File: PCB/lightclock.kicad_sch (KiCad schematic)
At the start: 187 parts, among them M1 Fan, Q1 NPN, Q2 AO3401A, Q3 AO3400A, SW1 TP15822637, U1 STP24DP05BTR, U11 TPS54232DR, U12 MPR121QR2, U13 PM254-1-06-W-8.5, U2 CH224K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

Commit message: added spare GPIO pads & ventilation for enclosure back
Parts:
- added GP24, GP25, GP26, GP27: ExtraGPIO, TestPoint:TestPoint_THTPad_1.5x1.5mm_Drill0.7mm, symbol Connector:TestPoint
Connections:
- net at U4.36 (GPIO24): now also GP24.1
- net at U4.37 (GPIO25): now also GP25.1
- net at U4.38 (GPIO26/ADC0): now also GP26.1
- net at U4.39 (GPIO27/ADC1): now also GP27.1
- no-connect marks 39 -> 35

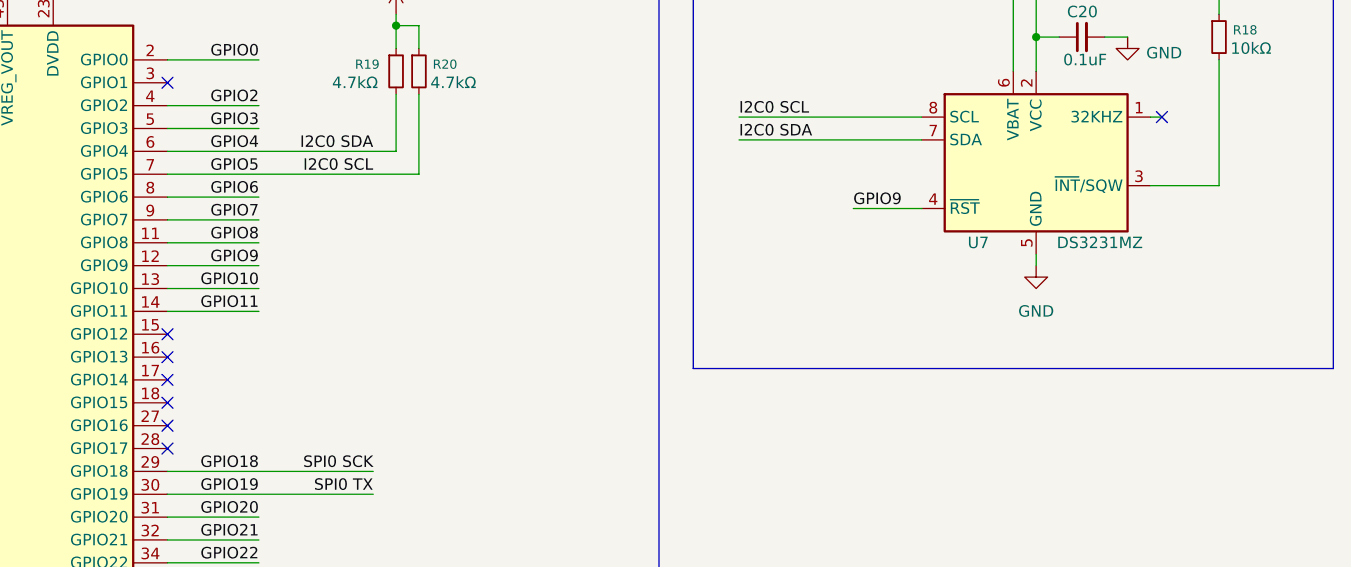
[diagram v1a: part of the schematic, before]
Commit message: connected INT pin on RTC to RP2040 for alarms
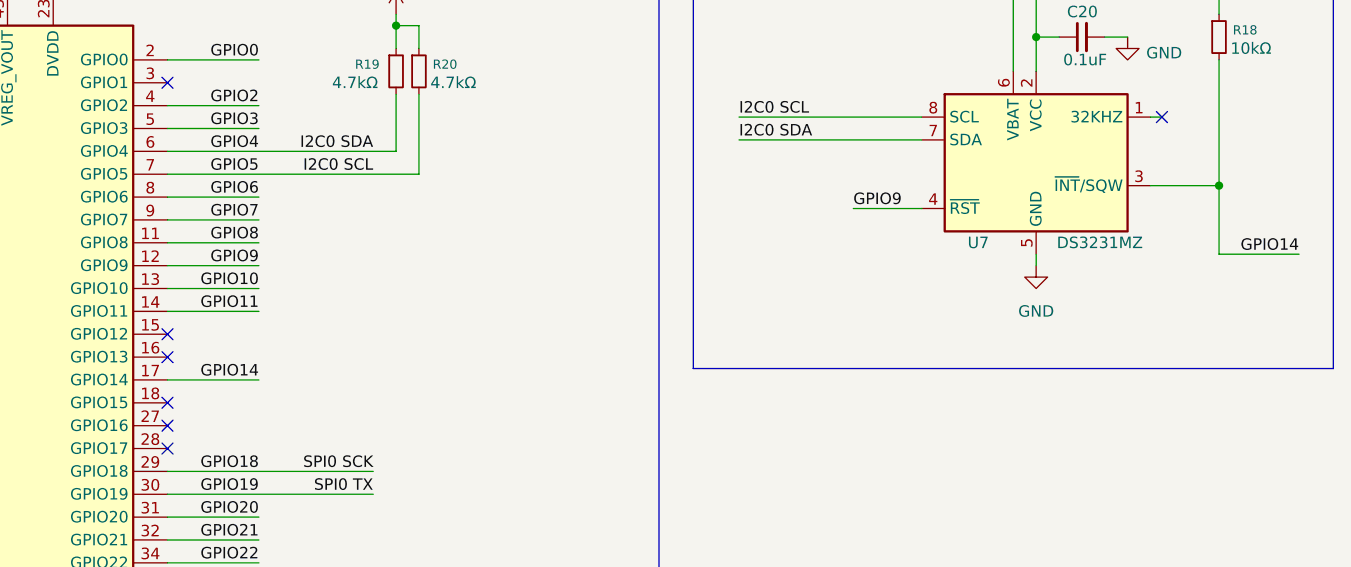
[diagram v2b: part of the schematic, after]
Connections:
- net GPIO14: now reaches R18.2, U7.3 (~{INT}/SQW)
- net GPIO14: now also U4.17 (GPIO14)
- no-connect marks 35 -> 34
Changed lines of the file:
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@@
 	)
 	(junction
+		(at 472.44 72.39)
+		(diameter 0)
+		(color 0 0 0 0)
+	)
+	(junction
 		(at 73.66 227.33)
 		(diameter 0)
@@
 	)
 	(no_connect
-		(at 355.6 93.98)
-	)
-	(no_connect
 		(at 435.61 210.82)
 	)
@@
 	(wire
 		(pts
+			(xy 365.76 93.98) (xy 355.6 93.98)
+		)
+		(stroke
+			(width 0)
+			(type default)
+		)
+	)
+	(wire
+		(pts
 			(xy 118.11 171.45) (xy 105.41 171.45)
 		)
@@
 	(wire
 		(pts
+			(xy 472.44 80.01) (xy 472.44 72.39)
+		)
+		(stroke
+			(width 0)
+			(type default)
+		)
+	)
+	(wire
+		(pts
 			(xy 59.69 76.2) (xy 62.23 76.2)
 		)
@@
 	(wire
 		(pts
+			(xy 472.44 80.01) (xy 481.33 80.01)
+		)
+		(stroke
+			(width 0)
+			(type default)
+		)
+	)
+	(wire
+		(pts
 			(xy 313.69 40.64) (xy 313.69 39.37)
 		)
@@
 		)
 	)
+	(label "GPIO14"
+		(at 481.33 80.01 180)
+		(effects
+			(font
+				(size 1.27 1.27)
+			)
+			(justify right bottom)
+		)
+	)
 	(label "QSPI_SD3"
 		(at 283.21 64.77 180)
@@
 		(effects
 			(font
+				(size 1.27 1.27)
+			)
+			(justify right bottom)
+		)
+	)
+	(label "GPIO14"
+		(at 365.76 93.98 180)
+		(effects
+			(font
